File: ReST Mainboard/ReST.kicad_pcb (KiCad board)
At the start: 2 copper layers, 109 parts, among them IC1 AT24C128, P1 USB_OTG, P10 CONN_01X04, P11 CONN_01X03, P12 CONN_02X04, P13 CONN_02X04, P14 CONN_02X10, P15 CONN_02X07, P16 CONN_02X04, P17 CONN_01X03, P18 CONN_01X03, P19 CONN_01X03, P2 CONN_01X02, P20 CONN_01X03, P21 CONN_02X10, P22 CONN_01X03, P23 SCREW_01X03, P24 CONN_01X03, P25 SCREW_01X03, P26 CONN_01X03, P27 SCREW_01X03, P28 CONN_01X03, P29 SCREW_01X03, P3 CONN_01X04, P30 CONN_01X03, P31 SCREW_01X03, P32 CONN_01X03, P33 SCREW_01X03, P34 CONN_01X03, P35 SCREW_01X04, P36 SCREW_01X04, P37 SCREW_01X04, P38 SCREW_01X04, P39 SCREW_01X04, P4 CONN_01X03, P40 SCREW_01X04, P41 CONN_02X04, P42 CONN_02X04, P43 CONN_02X04, P44 CONN_02X04, P45 CONN_02X04, P46 CONN_02X04, P47 CONN_02X03, P48 CONN_02X03, P49 CONN_02X03, P5 CONN_01X03, P50 CONN_02X03, P51 CONN_02X03, P52 CONN_02X03, P53 CONN_02X07, P54 CONN_01X03, P6 CONN_01X05, P7 CONN_02X05, P8 CONN_02X05, P9 CONN_01X04, SW1 SW-SPST-NO, U1 USBLC6-2, U10 POLOLU_A4988, U2 STM32F103VE, U3 L7805ACD2T-TR, U4 LM2574N-ADJ, U5 POLOLU_A4988, U6 POLOLU_A4988, U7 POLOLU_A4988, U8 POLOLU_A4988, U9 POLOLU_A4988, X1 8MHZ RESONATOR

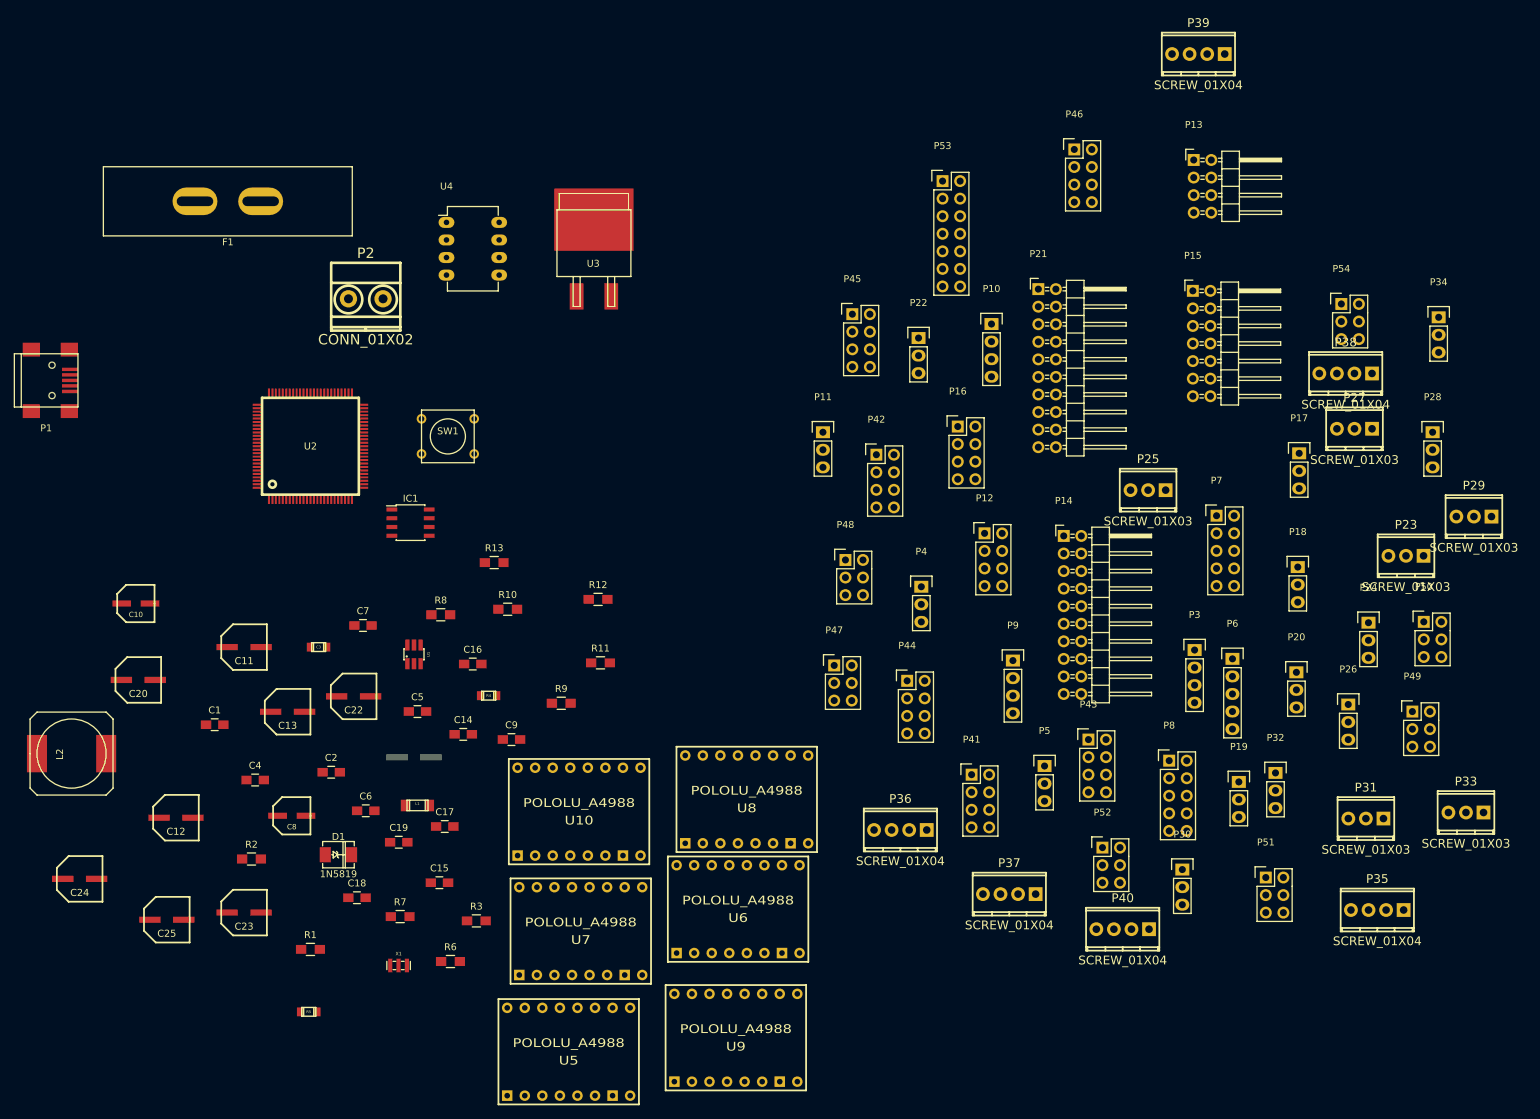
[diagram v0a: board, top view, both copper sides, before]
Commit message: PRE-RELEASE Rev. A!
Yay. I managed to finish the Main PCB over the night, must say, Im happy with it. Things that changed since the last release:

Heater:
-Heater Module uses less Pins
- Much smaller Design now

Heatbed & Additional Module: 
-Changed distance from Edge to first Pin from 2.5mm to 2mm (will be changed on other boards too)

Mainboard:
-Added I2C Pullups 4K7
-Swapped Pins from Stepper, Heaters and Endstops around for easier PCB Design.
-Finished Design (10cm x 10cm!)

Added some 3D Models for testing. If someone has problems with loading some modules, please contact me! (or make a pull request with a better solution)
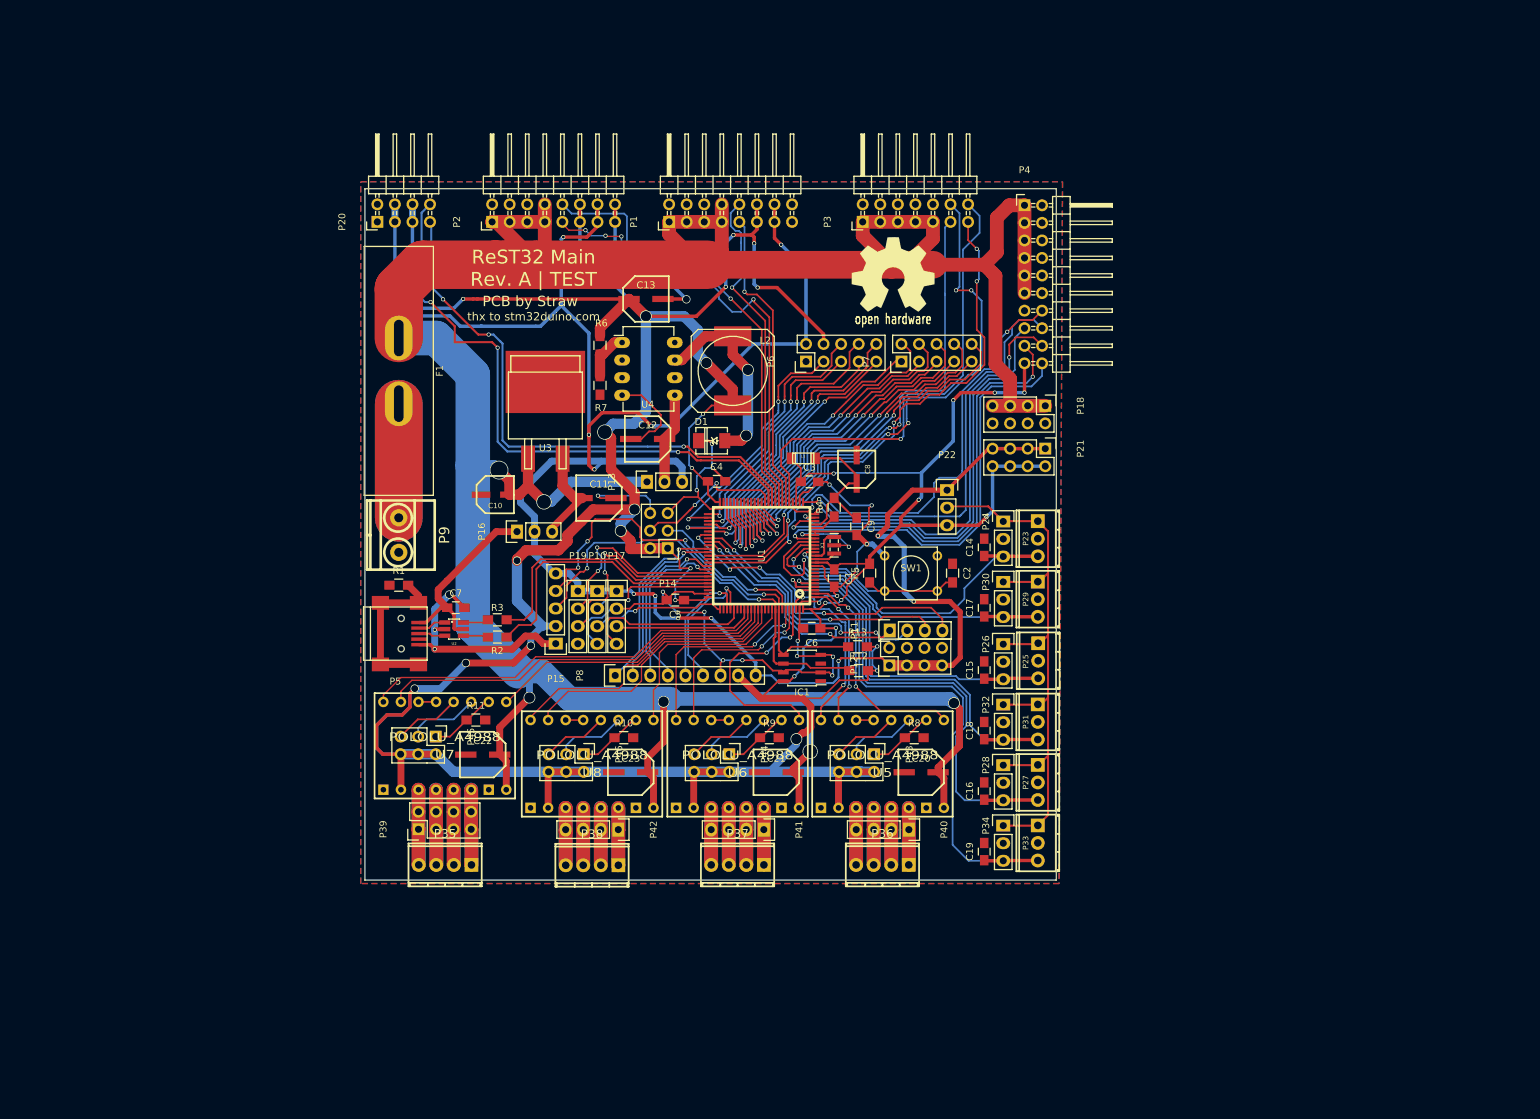
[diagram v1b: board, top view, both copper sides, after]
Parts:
- removed C24, C25: 100uF, ok-polcaps-panasonic:CP-PANASONIC-SMT_D8
- removed P47, P48, P49, P50, P51, P52: CONN_02X03, Pin_Headers:Pin_Header_Straight_2x03
- removed P53: CONN_02X07, Pin_Headers:Pin_Header_Straight_2x07
- removed P54: CONN_01X03, Pin_Headers:Pin_Header_Straight_2x03
- removed U10, U9: POLOLU_A4988, ReST-Library:SWDIP8_.6W
- added ?: , ReST-Library:Logo_silk_OSHW_12x13mm, F.Cu at (175.8, 67.8)
- C2: footprint Capacitors_SMD:C_0805_HandSoldering -> Resistors_SMD:R_0805_HandSoldering
- C21: moved to F.Cu
- C3: footprint ok-smd-generic:0805 -> Capacitors_SMD:C_0805_HandSoldering
- P1: value USB_OTG -> CONN_02X08; footprint Connect:USB_Mini-B -> Pin_Headers:Pin_Header_Angled_2x08
- P11, P17, P19: value CONN_01X03 -> CONN_01X04; footprint Pin_Headers:Pin_Header_Straight_1x03 -> Pin_Headers:Pin_Header_Straight_1x04
- P13: value CONN_02X04 -> CONN_01X03; footprint Pin_Headers:Pin_Header_Angled_2x04 -> Pin_Headers:Pin_Header_Straight_1x03
- P14: value CONN_02X10 -> CONN_02X03; footprint Pin_Headers:Pin_Header_Angled_2x10 -> Pin_Headers:Pin_Header_Straight_2x03
- P15: value CONN_02X07 -> CONN_01X05; footprint Pin_Headers:Pin_Header_Angled_2x07 -> Pin_Headers:Pin_Header_Straight_1x05
- P16: value CONN_02X04 -> CONN_01X03; footprint Pin_Headers:Pin_Header_Straight_2x04 -> Pin_Headers:Pin_Header_Straight_1x03
- P18: value CONN_01X03 -> CONN_02X04; footprint Pin_Headers:Pin_Header_Straight_1x03 -> Pin_Headers:Pin_Header_Straight_2x04
- P2: value CONN_01X02 -> CONN_02X08; footprint 5mm-pitch-terminal:mkds_1,5-2 -> Pin_Headers:Pin_Header_Angled_2x08
- P20: value CONN_01X03 -> CONN_02X04; footprint Pin_Headers:Pin_Header_Straight_1x03 -> Pin_Headers:Pin_Header_Angled_2x04
- P21: value CONN_02X10 -> CONN_02X04; footprint Pin_Headers:Pin_Header_Angled_2x10 -> Pin_Headers:Pin_Header_Straight_2x04
- P3: value CONN_01X04 -> CONN_02X07; footprint Pin_Headers:Pin_Header_Straight_1x04 -> Pin_Headers:Pin_Header_Angled_2x07
- P39: value SCREW_01X04 -> CONN_02X04; footprint 2:mpt_0,5%2f4-2,54 -> Pin_Headers:Pin_Header_Straight_2x04
- P4: value CONN_01X03 -> CONN_02X10; footprint Pin_Headers:Pin_Header_Straight_1x03 -> Pin_Headers:Pin_Header_Angled_2x10
- P40: value SCREW_01X04 -> CONN_01X04; footprint 2:mpt_0,5%2f4-2,54 -> Pin_Headers:Pin_Header_Straight_1x04
- P41, P42: value CONN_02X04 -> CONN_01X04; footprint Pin_Headers:Pin_Header_Straight_2x04 -> Pin_Headers:Pin_Header_Straight_1x04
- P43, P44, P45, P46: value CONN_02X04 -> CONN_02X03; footprint Pin_Headers:Pin_Header_Straight_2x04 -> Pin_Headers:Pin_Header_Straight_2x03
- P5: value CONN_01X03 -> USB_OTG; footprint Pin_Headers:Pin_Header_Straight_1x03 -> Connect:USB_Mini-B
- P6: value CONN_01X05 -> CONN_02X05; footprint Pin_Headers:Pin_Header_Straight_1x05 -> Pin_Headers:Pin_Header_Straight_2x05
- P8: value CONN_02X05 -> CONN_01X09; footprint Pin_Headers:Pin_Header_Straight_2x05 -> Pin_Headers:Pin_Header_Straight_1x09
- P9: value CONN_01X04 -> CONN_01X02; footprint Pin_Headers:Pin_Header_Straight_1x04 -> 5mm-pitch-terminal:mkds_1,5-2
- R12, R13: value 100K -> 4K7
- R4, R5: footprint ok-smd-generic:0805 -> Resistors_SMD:R_0805_HandSoldering
- U1: value USBLC6-2 -> STM32F103VE; footprint ReST-Library:SOT32-6L -> ok-ic-smd:LQFP100-14x14
- U2: value STM32F103VE -> USBLC6-2; footprint ok-ic-smd:LQFP100-14x14 -> ReST-Library:SOT32-6L
- moved P39 159.0 mm to (107.2, 148.1), turned to 90 degrees
- moved P20 148.0 mm to (101.2, 60.2), turned to 90 degrees
- moved P35 135.0 mm to (111.0, 153.2)
- moved P38 130.2 mm to (132.3, 153.3)
- moved C20 114.0 mm to (179.9, 139.8), turned to 180 degrees
- moved P46 112.6 mm to (131.1, 137.2), turned to 270 degrees
- moved L2 110.5 mm to (152.7, 81.8), turned to 270 degrees
- moved P15 105.3 mm to (127.0, 121.2), turned to 180 degrees
- moved R5 103.0 mm to (172.4, 111.0), turned to 90 degrees
- moved P17 100.7 mm to (135.8, 113.7)
- moved P19 99.5 mm to (130.2, 113.7)
- moved P34 96.8 mm to (191.8, 147.6)
- moved C8 95.9 mm to (170.6, 96.0), turned to 90 degrees
- moved P5 95.8 mm to (103.8, 119.8)
- moved C2 94.4 mm to (184.4, 111.0), turned to 270 degrees
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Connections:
- C1 pad 1: VCC -> +3V3
- C2 pad 1: +3V3 -> GND
- C2 pad 2: GND -> Net-(C2-Pad2)
- C3 pad 1: GND -> +3V3
- C3 pad 2: Net-(C3-Pad2) -> GND
- C7 pad 1: +3V3 -> VCC
- P1 pad 1: VCC -> +12V
- P1 pad 2: Net-(P1-Pad2) -> GND
- P1 pad 3: Net-(P1-Pad3) -> +12V
- P1 pad 4: (no net) -> GND
- P1 pad 5: GND -> +12V
- P1 pad 6: Net-(P1-Pad6) -> GND
- P10 pad 2: /UART1-TX -> /SWDIO
- P10 pad 3: /UART1-RX -> /SWCLK
- P11 pad 1: +12V -> /SERVO4
- P11 pad 2: VAA -> /SERVO3
- P11 pad 3: +5V -> /SERVO2
- P12 pad 1: +12V -> +5V
- P12 pad 3: +12V -> +5V
- P12 pad 5: +12V -> +5V
- P12 pad 7: +12V -> +5V
- P13 pad 1: GND -> +12V
- P13 pad 2: GND -> VAA
- P14 pad 1: +12V -> +3V3
- P14 pad 2: GND -> +3V3
- P14 pad 3: +12V -> /BOOT0
- P14 pad 4: GND -> /BOOT1
- P14 pad 5: +12V -> GND
- P15 pad 1: +12V -> GND
- P15 pad 2: GND -> +3V3
- P15 pad 3: +12V -> /I2C-SCL
- P15 pad 4: GND -> /I2C-SDA
- P15 pad 5: +12V -> +5V
- P16 pad 1: +5V -> VCC
- P16 pad 2: +3V3 -> +5V
- P16 pad 3: +5V -> VCC/2
- P17 pad 1: /SERVO1 -> +5V
- P17 pad 2: +5V -> GND
- P17 pad 3: GND -> /UART5-RX
- P18 pad 1: /SERVO3 -> +12V
- P18 pad 2: +5V -> GND
- P18 pad 3: GND -> +12V
- P19 pad 1: /SERVO2 -> +5V
- P19 pad 2: +5V -> /UART1-TX
- P19 pad 3: GND -> /UART1-RX
- P2 pad 1: Net-(F1-Pad1) -> +12V
- P20 pad 1: /SERVO4 -> GND
- P20 pad 2: +5V -> GND
- P20 pad 3: GND -> +5V
- P21 pad 1: +12V -> +5V
- P21 pad 2: GND -> +3V3
- P21 pad 3: +12V -> +5V
- P21 pad 4: GND -> +3V3
- P21 pad 5: +12V -> +5V
- P21 pad 6: GND -> +3V3
- P21 pad 7: +12V -> +5V
- P21 pad 8: GND -> +3V3
- P22 pad 1: VCC -> +5V
- P22 pad 2: +5V -> /ENDSTOP_VCC
- P22 pad 3: VCC/2 -> +3V3
- P3 pad 1: +5V -> +12V
- P3 pad 2: /SWCLK -> GND
- P3 pad 3: GND -> +12V
- P3 pad 4: /SWDIO -> GND
- P39 pad 1: Net-(P39-Pad1) -> Net-(P35-Pad4)
- P39 pad 2: Net-(P39-Pad2) -> Net-(P35-Pad4)
- P39 pad 3: Net-(P39-Pad3) -> Net-(P35-Pad3)
- P39 pad 4: Net-(P39-Pad4) -> Net-(P35-Pad3)
- P4 pad 1: +3V3 -> +12V
- P4 pad 2: /BOOT0 -> GND
- P4 pad 3: GND -> +12V
- P40 pad 1: Net-(P40-Pad1) -> Net-(P36-Pad1)
- P40 pad 2: Net-(P40-Pad2) -> Net-(P36-Pad2)
- P40 pad 3: Net-(P40-Pad3) -> Net-(P36-Pad3)
- P40 pad 4: Net-(P40-Pad4) -> Net-(P36-Pad4)
- P41 pad 1: Net-(P35-Pad4) -> Net-(P37-Pad1)
- P41 pad 2: Net-(P41-Pad2) -> Net-(P37-Pad2)
- P41 pad 3: Net-(P35-Pad3) -> Net-(P37-Pad3)
- P41 pad 4: Net-(P41-Pad4) -> Net-(P37-Pad4)
- P42 pad 1: Net-(P36-Pad4) -> Net-(P38-Pad1)
- P42 pad 2: Net-(P42-Pad2) -> Net-(P38-Pad2)
- P42 pad 3: Net-(P36-Pad3) -> Net-(P38-Pad3)
- P42 pad 4: Net-(P42-Pad4) -> Net-(P38-Pad4)
- P43 pad 1: Net-(P37-Pad4) -> Net-(P43-Pad1)
- P43 pad 2: Net-(P43-Pad2) -> +3V3
- P43 pad 3: Net-(P37-Pad3) -> Net-(P43-Pad3)
- P43 pad 4: Net-(P43-Pad4) -> +3V3
- P43 pad 5: Net-(P37-Pad2) -> Net-(P43-Pad5)
- P43 pad 6: Net-(P43-Pad6) -> +3V3
- P44 pad 1: Net-(P38-Pad4) -> Net-(P44-Pad1)
- P44 pad 2: Net-(P44-Pad2) -> +3V3
- P44 pad 3: Net-(P38-Pad3) -> Net-(P44-Pad3)
- P44 pad 4: Net-(P44-Pad4) -> +3V3
- P44 pad 5: Net-(P38-Pad2) -> Net-(P44-Pad5)
- P44 pad 6: Net-(P44-Pad6) -> +3V3
- P45 pad 1: Net-(P39-Pad4) -> Net-(P45-Pad1)
- P45 pad 2: Net-(P45-Pad2) -> +3V3
- P45 pad 3: Net-(P39-Pad3) -> Net-(P45-Pad3)
- P45 pad 4: Net-(P45-Pad4) -> +3V3
- P45 pad 5: Net-(P39-Pad2) -> Net-(P45-Pad5)
- P45 pad 6: Net-(P45-Pad6) -> +3V3
- P46 pad 1: Net-(P40-Pad4) -> Net-(P46-Pad1)
- P46 pad 2: Net-(P46-Pad2) -> +3V3
- P46 pad 3: Net-(P40-Pad3) -> Net-(P46-Pad3)
- P46 pad 4: Net-(P46-Pad4) -> +3V3
- P46 pad 5: Net-(P40-Pad2) -> Net-(P46-Pad5)
- P46 pad 6: Net-(P46-Pad6) -> +3V3
- P5 pad 1: +3V3 -> VCC
- P5 pad 2: /BOOT1 -> Net-(P5-Pad2)
- P5 pad 3: GND -> Net-(P5-Pad3)
- P6 pad 2: +3V3 -> +5V
- P6 pad 3: /I2C-SCL -> /SPI-SCK
- P6 pad 4: /I2C-SDA -> +3V3
- P6 pad 5: +5V -> /SPI-MISO
- P7 pad 1: GND -> /LCD-CD
- P7 pad 10: /LCD-RD -> /LCD-D0
- P7 pad 2: +5V -> /LCD-CS
- P7 pad 3: /SPI-SCK -> /LCD-D7
- P7 pad 4: +3V3 -> /LCD-D6
- P7 pad 5: /SPI-MISO -> /LCD-D5
- P7 pad 6: /SPI-CS1 -> /LCD-D4
- P7 pad 7: /SPI-MOSI -> /LCD-D3
- P7 pad 8: /SPI-CS2 -> /LCD-D2
- P7 pad 9: /LCD-WR -> /LCD-D1
- P8 pad 1: /LCD-CD -> /EXTRA0
- P8 pad 2: /LCD-CS -> /EXTRA1
- P8 pad 3: /LCD-D7 -> /EXTRA2
- P8 pad 4: /LCD-D6 -> /EXTRA3
- P8 pad 5: /LCD-D5 -> /EXTRA4
- P8 pad 6: /LCD-D4 -> /EXTRA5
- P8 pad 7: /LCD-D3 -> GND
- P8 pad 8: /LCD-D2 -> +3V3
- P8 pad 9: /LCD-D1 -> +5V
- P9 pad 1: +5V -> Net-(F1-Pad1)
- R1 pad 2: Net-(P1-Pad6) -> Net-(P5-Pad6)
- R10 pad 1: Net-(P49-Pad5) -> Net-(P46-Pad1)
- R11 pad 1: Net-(P50-Pad5) -> Net-(P45-Pad1)
- R12 pad 1: Net-(P51-Pad5) -> /I2C-SCL
- R12 pad 2: GND -> +3V3
- R13 pad 1: Net-(P52-Pad5) -> /I2C-SDA
- R13 pad 2: GND -> +3V3
- R2 pad 2: /USBDM -> /USBDP
- R3 pad 1: /USBDP -> /USBDM
- R5 pad 1: Net-(C3-Pad2) -> Net-(C2-Pad2)
- R8 pad 1: Net-(P47-Pad5) -> Net-(P43-Pad1)
- R9 pad 1: Net-(P48-Pad5) -> Net-(P44-Pad1)
- SW1 pad 2: Net-(C3-Pad2) -> Net-(C2-Pad2)
- U1 pad 1: Net-(P1-Pad3) -> /X-STEP
- U1 pad 2: GND -> /X-EN
- U1 pad 3: Net-(P1-Pad2) -> /Z-MAX
- U1 pad 4: Net-(R2-Pad1) -> /Z-MIN
- U1 pad 5: VCC -> /Y-MAX
- U1 pad 6: Net-(R3-Pad2) -> (no net)
- U2 pad 1: /Y-STEP -> Net-(P5-Pad2)
- U2 pad 2: /Y-EN -> GND
- U2 pad 3: /Z-DIR -> Net-(P5-Pad3)
- U2 pad 4: /Z-STEP -> Net-(R2-Pad1)
- U2 pad 5: /Z-EN -> VCC
- U2 pad 6: (no net) -> Net-(R3-Pad2)
- U5 pad 10: Net-(P47-Pad5) -> Net-(P43-Pad1)
- U5 pad 11: Net-(P47-Pad3) -> Net-(P43-Pad3)
- U5 pad 12: Net-(P47-Pad1) -> Net-(P43-Pad5)
- U5 pad 3: Net-(P41-Pad2) -> Net-(P36-Pad4)
- U5 pad 4: Net-(P41-Pad4) -> Net-(P36-Pad3)
- U5 pad 5: Net-(P41-Pad6) -> Net-(P36-Pad2)
- U5 pad 6: Net-(P41-Pad8) -> Net-(P36-Pad1)
- U6 pad 10: Net-(P48-Pad5) -> Net-(P44-Pad1)
- U6 pad 11: Net-(P48-Pad3) -> Net-(P44-Pad3)
- U6 pad 12: Net-(P48-Pad1) -> Net-(P44-Pad5)
- U6 pad 3: Net-(P42-Pad2) -> Net-(P37-Pad4)
- U6 pad 4: Net-(P42-Pad4) -> Net-(P37-Pad3)
- U6 pad 5: Net-(P42-Pad6) -> Net-(P37-Pad2)
- U6 pad 6: Net-(P42-Pad8) -> Net-(P37-Pad1)
- U7 pad 10: Net-(P49-Pad5) -> Net-(P45-Pad1)
- U7 pad 11: Net-(P49-Pad3) -> Net-(P45-Pad3)
- U7 pad 12: Net-(P49-Pad1) -> Net-(P45-Pad5)
- U7 pad 3: Net-(P43-Pad2) -> Net-(P35-Pad4)
- U7 pad 4: Net-(P43-Pad4) -> Net-(P35-Pad3)
- U7 pad 5: Net-(P43-Pad6) -> Net-(P35-Pad2)
- U7 pad 6: Net-(P43-Pad8) -> Net-(P35-Pad1)
- U8 pad 10: Net-(P50-Pad5) -> Net-(P46-Pad1)
- U8 pad 11: Net-(P50-Pad3) -> Net-(P46-Pad3)
- U8 pad 12: Net-(P50-Pad1) -> Net-(P46-Pad5)
- U8 pad 3: Net-(P44-Pad2) -> Net-(P38-Pad4)
- U8 pad 4: Net-(P44-Pad4) -> Net-(P38-Pad3)
- U8 pad 5: Net-(P44-Pad6) -> Net-(P38-Pad2)
- U8 pad 6: Net-(P44-Pad8) -> Net-(P38-Pad1)
- X1 pad 1: Net-(U2-Pad12) -> Net-(U1-Pad12)
- X1 pad 2: Net-(U2-Pad13) -> Net-(U1-Pad13)
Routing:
- net +3V3: track 0.00 -> 625.2 mm, vias 0 -> 31
- net +12V: track 0.00 -> 472.4 mm, vias 0 -> 6
- net +5V: track 0.00 -> 319.3 mm, vias 0 -> 12
- net GND: track 0.00 -> 248.3 mm, vias 0 -> 25
- net /ENDSTOP_VCC: track 0.00 -> 92.3 mm
- net /PWM-BED: track 0.00 -> 86.8 mm, vias 0 -> 3
- net /PWM-ADD2: track 0.00 -> 83.3 mm, vias 0 -> 5
- net /T0: track 0.00 -> 81.0 mm, vias 0 -> 3
- net /PWM-ADD1: track 0.00 -> 78.8 mm, vias 0 -> 4
- net /Z-MAX: track 0.00 -> 76.1 mm, vias 0 -> 1
- net /PWM-ADD3: track 0.00 -> 74.3 mm, vias 0 -> 3
- net /Z-MIN: track 0.00 -> 71.7 mm, vias 0 -> 1
- net /PWM-ADD0: track 0.00 -> 68.6 mm, vias 0 -> 1
- net /PWM-HEAT0: track 0.00 -> 66.1 mm, vias 0 -> 4
- net /E1-STEP: track 0.00 -> 64.6 mm, vias 0 -> 2
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- added copper zone on B.Cu, net GND
- added copper zone on F.Cu, net GND
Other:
- board outline added: 100 x 100 mm
- net class Default: clearance 0.2 -> 0.1524
- rule trace_clearance: 0.2 -> 0.1524
- rule trace_min: 0.2 -> 0.1524
- rule via_min_size: 0.4 -> 0.16
- board text added: "PCB by Straw"
- board text added: "ReST32 Main Rev. A | TEST"
- board text added: "thx to stm32duino.com"

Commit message: Added Images and PDF's
+ Silkscreening
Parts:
- added G***: LOGO, ReST-Library:STM32-12mm, F.Cu at (166.0, 69.0)
- moved ? 4.37 mm to (180.2, 67.4)
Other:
- board text removed: "thx to stm32duino.com"

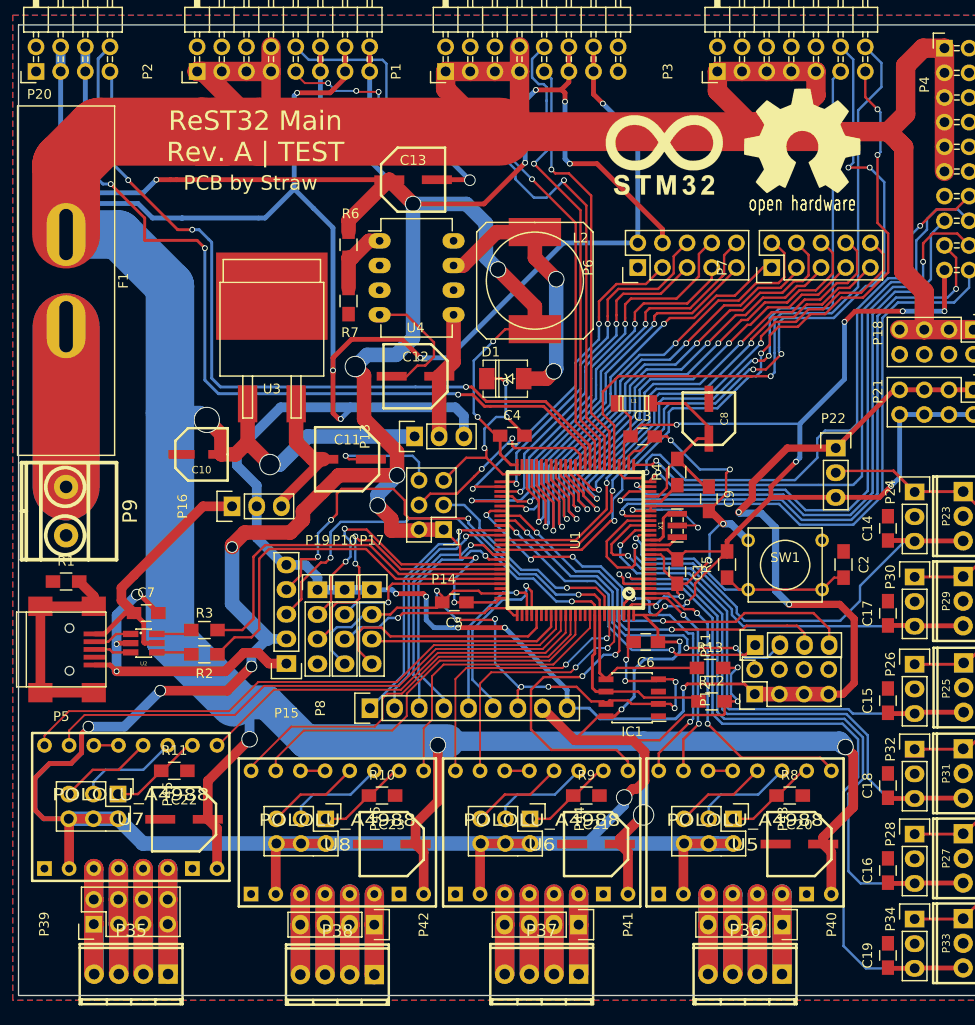
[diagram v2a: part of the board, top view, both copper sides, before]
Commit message: Added Mounting Holes to all Modules
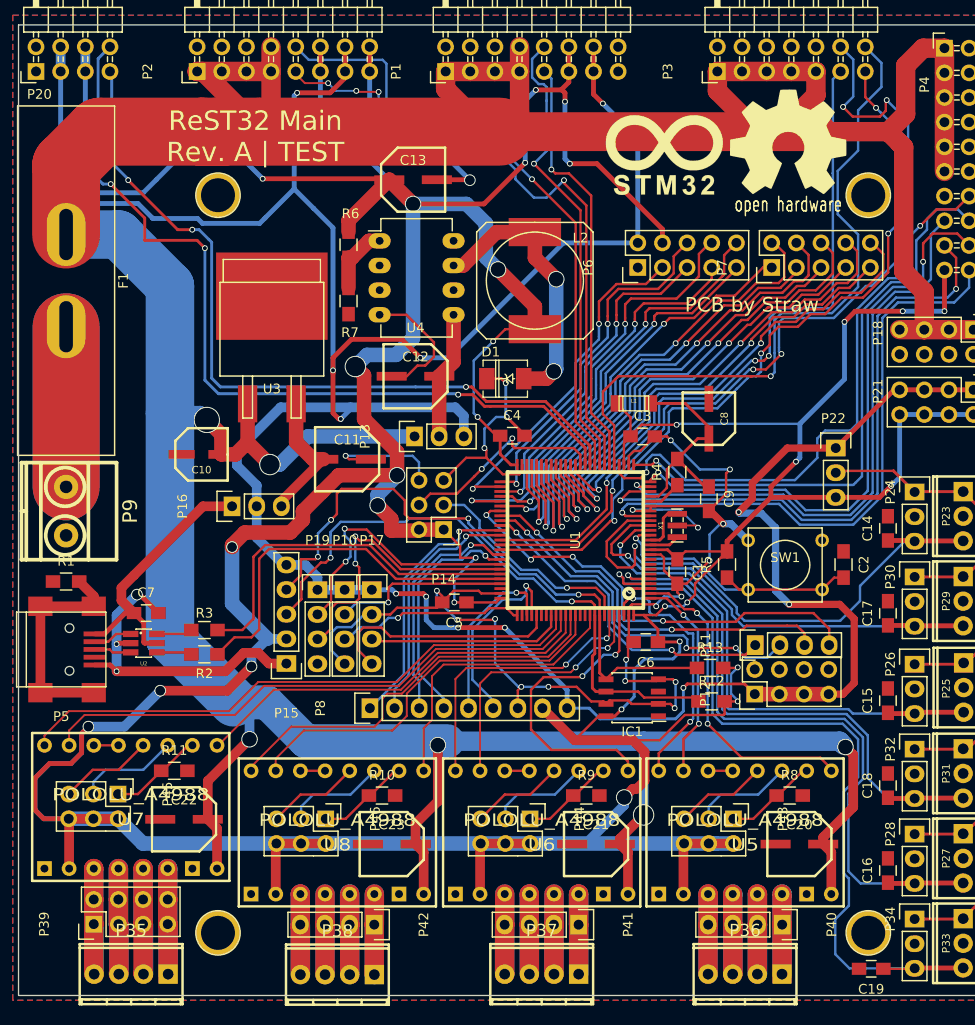
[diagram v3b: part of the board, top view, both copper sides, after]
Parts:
- added ?: , Connect:1pin, F.Cu at (120.0, 73.0)
- added ?: , Connect:1pin, F.Cu at (120.0, 149.0)
- added ?: , Connect:1pin, F.Cu at (187.0, 149.0)
- added ?: , Connect:1pin, F.Cu at (187.0, 73.0)
- moved C19 2.21 mm to (187.3, 152.7), turned to 180 degrees
- moved ? 1.45 mm to (178.8, 67.5)
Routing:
- net /PWM-ADD2: track 83.3 -> 89.5 mm
- net /Z-MAX: track 76.1 -> 78.6 mm
- net /PWM-ADD0: track 68.6 -> 70.3 mm
- net +3V3: track 625.2 -> 626.7 mm
- net /PWM-ADD1: track 78.8 -> 79.9 mm
